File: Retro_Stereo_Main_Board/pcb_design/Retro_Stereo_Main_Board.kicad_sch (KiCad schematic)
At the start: 29 parts, among them J1 BM23FR0.6-30DS-0.35V895, J2 USB_C_Receptacle, J3 1734366-1, J4 SD_Card_Receptacle, J5 TC2030, J6 Conn_01x04, J7 Conn_01x06, J8 Conn_01x06, SW1 RotaryEncoder_Switch_MP, SW9 SW_Push

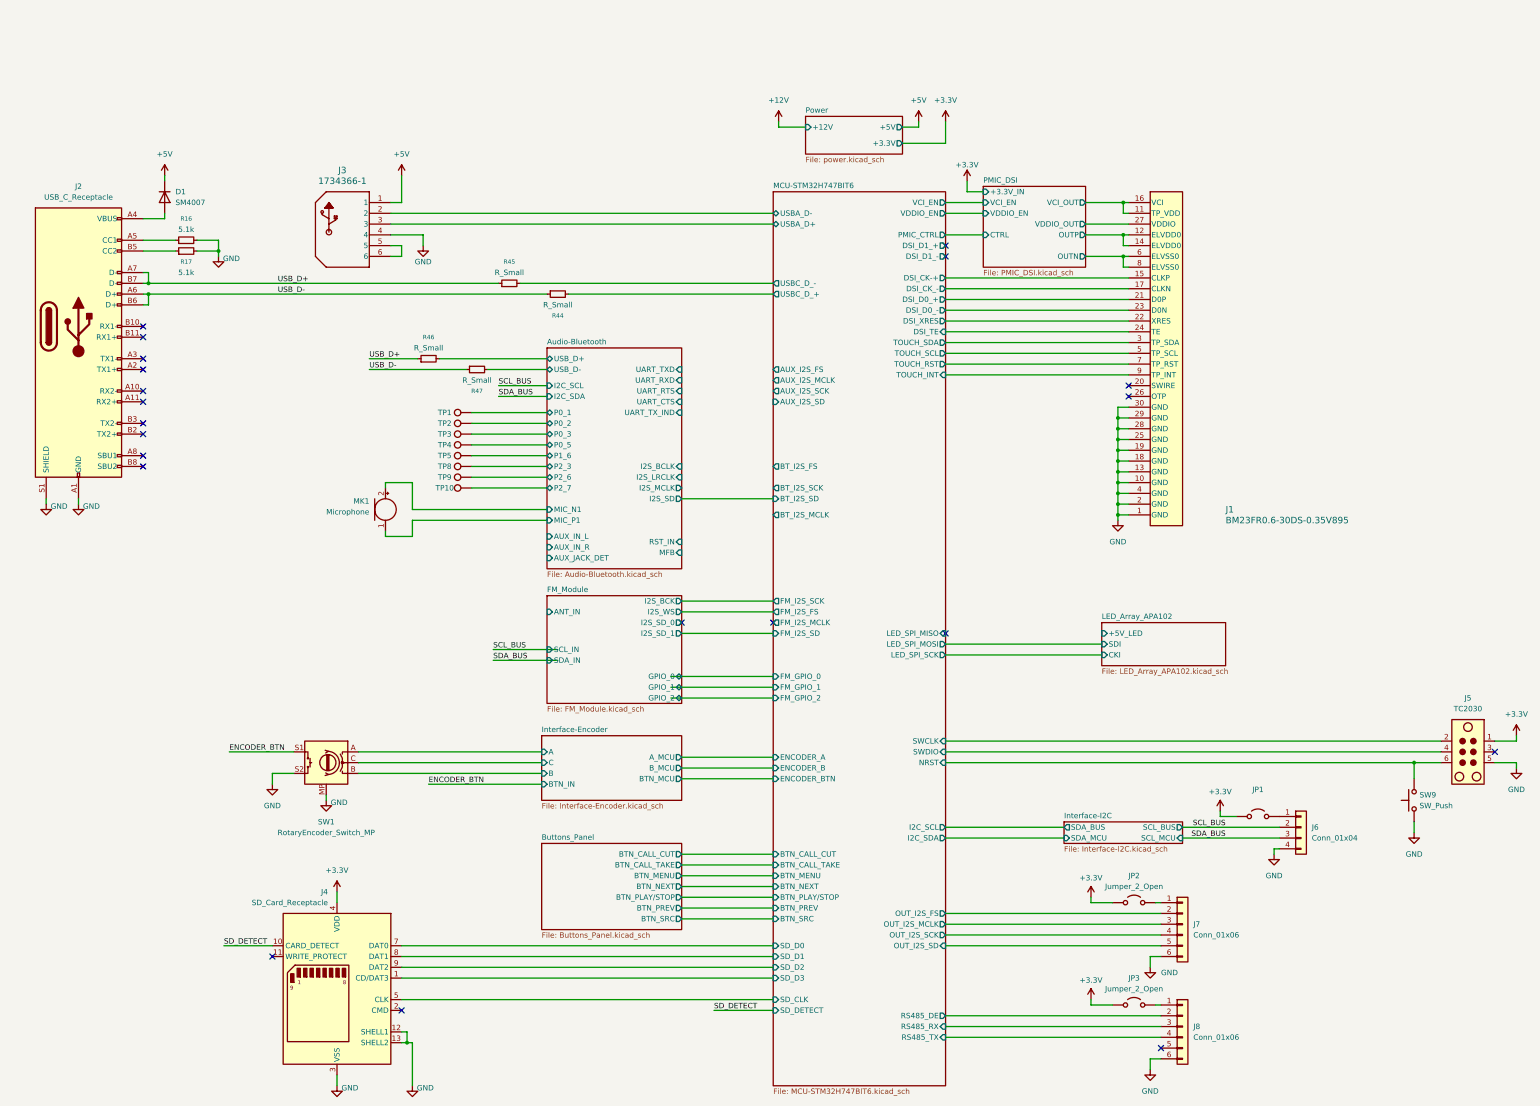
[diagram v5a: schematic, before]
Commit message: Add jumper resistors
Signed-off-by: Francisco <fran.testa07Qgmail.com>
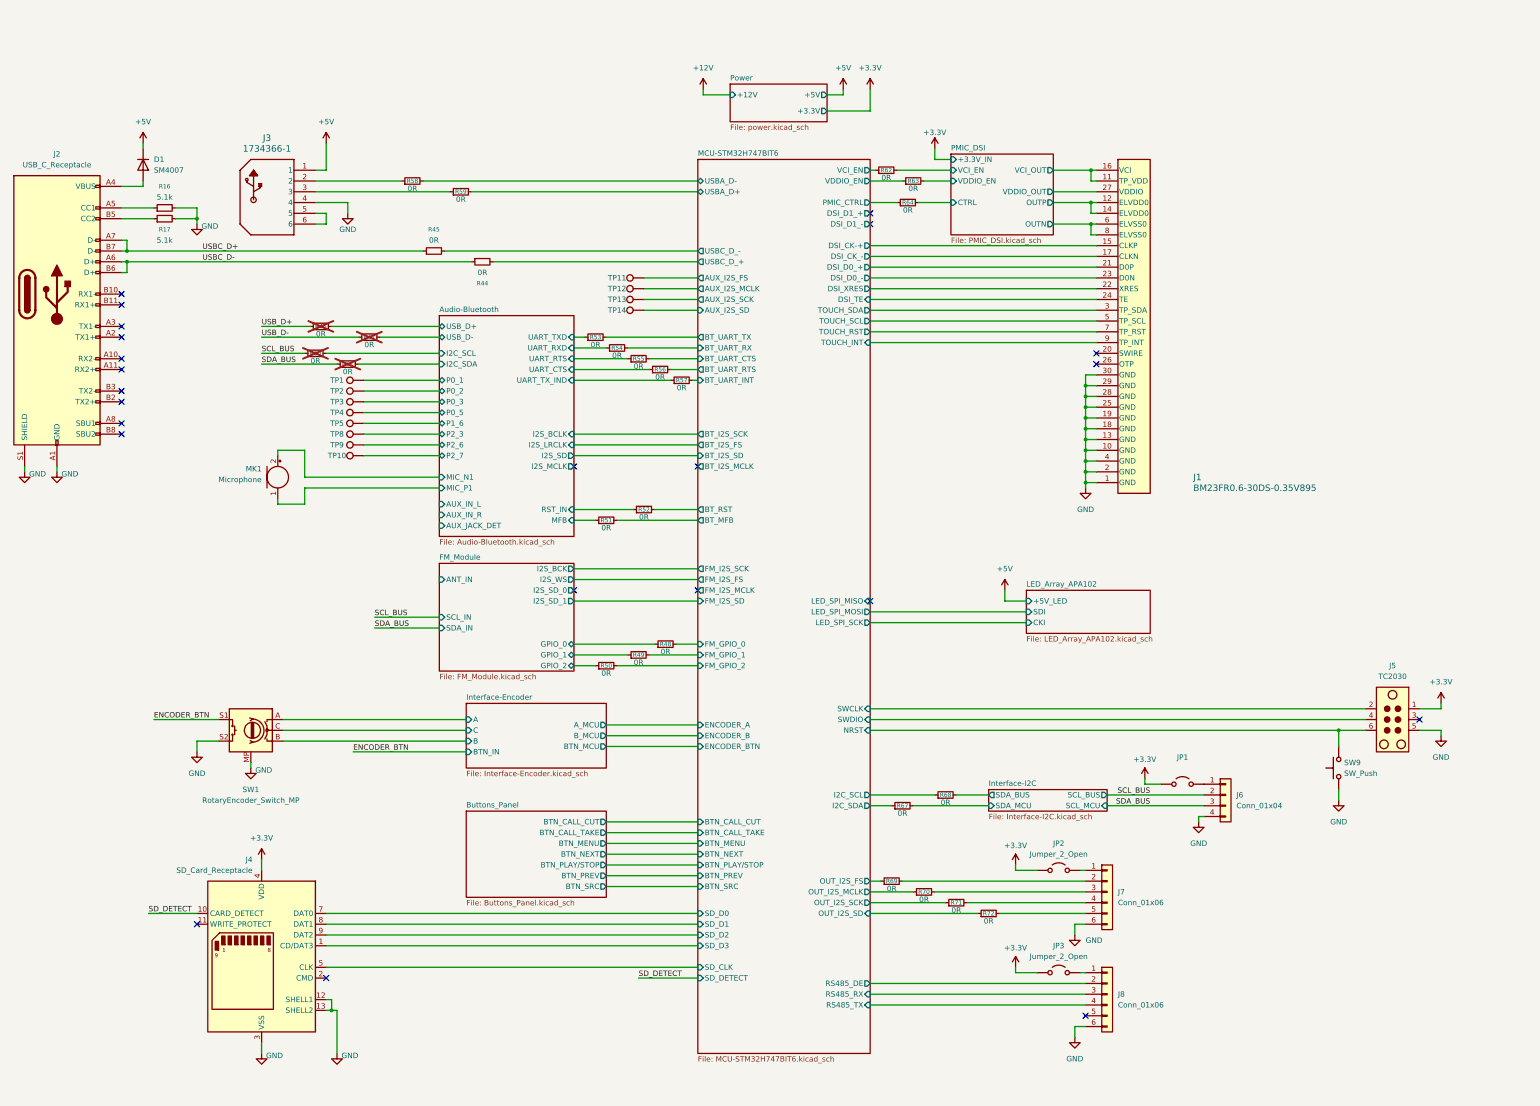
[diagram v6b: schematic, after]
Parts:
- added R48, R49, R50, R51, R52, R53, R54, R55, R56, R57, R58, R59, R60, R61, R62, R63, R64, R67, R68, R69, R70, R71, R72: 0R, symbol Device:R_Small
- added TP11, TP12, TP13, TP14: TestPoint, symbol Connector:TestPoint
- R44, R45: value R_Small -> 0R
- R46, R47: value R_Small -> 0R; now not fitted; now left out of the parts list
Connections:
- net Audio-Bluetooth/MFB: now also R51.1
- net Audio-Bluetooth/RST_IN: now also R52.1
- net Audio-Bluetooth/UART_CTS: now also R56.1
- net Audio-Bluetooth/UART_RTS: now also R55.1
- net Audio-Bluetooth/UART_RXD: now also R54.1
- net Audio-Bluetooth/UART_TXD: now also R53.1
- net Audio-Bluetooth/UART_TX_IND: now also R57.1
- net FM_Module/GPIO_0: now also R48.1
- net FM_Module/GPIO_1: now also R49.1
- net FM_Module/GPIO_2: now also R50.1
- net Interface-I2C/SDA_BUS: now also R68.2
- net Interface-I2C/SDA_MCU: now also R67.2
- net MCU-STM32H747BIT6/AUX_I2S_FS: now also TP11.1
- net MCU-STM32H747BIT6/AUX_I2S_MCLK: now also TP12.1
- net MCU-STM32H747BIT6/AUX_I2S_SCK: now also TP13.1
- net MCU-STM32H747BIT6/AUX_I2S_SD: now also TP14.1
- net MCU-STM32H747BIT6/FM_GPIO_0: now also R48.2
- net MCU-STM32H747BIT6/FM_GPIO_1: now also R49.2
- net MCU-STM32H747BIT6/FM_GPIO_2: now also R50.2
- net MCU-STM32H747BIT6/OUT_I2S_FS: now also R69.1; no longer J7.2 (Pin_2)
- net MCU-STM32H747BIT6/OUT_I2S_MCLK: now also R70.1; no longer J7.3 (Pin_3)
- net MCU-STM32H747BIT6/OUT_I2S_SCK: now also R71.1; no longer J7.4 (Pin_4)
- net MCU-STM32H747BIT6/OUT_I2S_SD: now also R72.1; no longer J7.5 (Pin_5)
- net MCU-STM32H747BIT6/PMIC_CTRL: now also R64.1
- net MCU-STM32H747BIT6/USBA_D+: now also R59.2; no longer J3.3
- net MCU-STM32H747BIT6/USBA_D-: now also R58.2; no longer J3.2
- net MCU-STM32H747BIT6/VCI_EN: now also R62.1
- net MCU-STM32H747BIT6/VDDIO_EN: now also R63.1
- net SCL_BUS: now also R60.1
- net SDA_BUS: now also R61.1
- net USB_D+: no longer J2.A7 (D-), J2.B7 (D-), R45.1
- net USB_D-: no longer J2.A6 (D+), J2.B6 (D+), R44.1
- new net: J7.3 (Pin_3), R70.2
- new net: J7.5 (Pin_5), R72.2
- new net: J7.2 (Pin_2), R69.2
- new net: J7.4 (Pin_4), R71.2
- new net: J3.3, R59.1
- new net: J3.2, R58.1
- new net Audio-Bluetooth/I2C_SCL: R60.2
- new net Audio-Bluetooth/I2C_SDA: R61.2
- new net MCU-STM32H747BIT6/BT_MFB: R51.2
- new net MCU-STM32H747BIT6/BT_RST: R52.2
- new net MCU-STM32H747BIT6/BT_UART_CTS: R55.2
- new net MCU-STM32H747BIT6/BT_UART_INT: R57.2
- new net MCU-STM32H747BIT6/BT_UART_RTS: R56.2
- new net MCU-STM32H747BIT6/BT_UART_RX: R54.2
- new net MCU-STM32H747BIT6/BT_UART_TX: R53.2
- new net MCU-STM32H747BIT6/I2C_SCL: R68.1
- new net MCU-STM32H747BIT6/I2C_SDA: R67.1
- new net PMIC_DSI/CTRL: R64.2
- new net PMIC_DSI/VCI_EN: R62.2
- new net PMIC_DSI/VDDIO_EN: R63.2
- new net USBC_D+: J2.A7 (D-), J2.B7 (D-), R45.1
- new net USBC_D-: J2.A6 (D+), J2.B6 (D+), R44.1
- no-connect marks 21 -> 23
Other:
- sheet MCU-STM32H747BIT6 ports: added BT_MFB, BT_RST, BT_UART_CTS, BT_UART_INT, BT_UART_RTS, BT_UART_RX, BT_UART_TX; removed none
- moved on the sheet: D1, J1, J2, J3, J4, J5, J6, J7, J8, JP1, JP2, JP3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
